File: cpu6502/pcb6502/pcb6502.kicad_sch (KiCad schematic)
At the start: 45 parts, among them J1 Power, J2 RS232, SW1 Reset, SW2 IRQ, SW3 Debug, U1 6502 (CPU), U2 28C256 (ROM), U3 62256 (RAM), U4 6522 (VIA), U5 74HC00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

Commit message: everything is working well!  OS still wip but pretty good
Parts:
- added J3: VIA PB, Connector_PinHeader_2.54mm:PinHeader_2x05_P2.54mm_Vertical, symbol Connector:Conn_01x10_Pin
- added J4: Reset Ext, Connector_PinHeader_2.54mm:PinHeader_1x02_P2.54mm_Vertical, symbol Connector:Conn_01x02_Pin
- C2, C3, C4, C5, C6: footprint Capacitor_THT:C_Disc_D3.0mm_W1.6mm_P2.50mm -> Capacitor_THT:C_Disc_D5.0mm_W2.5mm_P5.00mm
- R5: footprint Resistor_THT:R_Axial_DIN0204_L3.6mm_D1.6mm_P7.62mm_Horizontal -> Resistor_THT:R_Axial_DIN0204_L3.6mm_D1.6mm_P2.54mm_Vertical
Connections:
- net +5V: now also J3.9 (Pin_9)
- net GND: now also J3.10 (Pin_10), J4.2 (Pin_2)
- net RST: now also J4.1 (Pin_1)
- net PB0: now reaches U4.10 (PB0)
- net PB0: now also J3.1 (Pin_1)
- net PB1: now reaches U4.11 (PB1)
- net PB1: now also J3.2 (Pin_2)
- net PB2: now reaches U4.12 (PB2)
- net PB2: now also J3.3 (Pin_3)
- net PB3: now reaches U4.13 (PB3)
- net PB3: now also J3.4 (Pin_4)
- net PB4: now reaches U4.14 (PB4)
- net PB4: now also J3.5 (Pin_5)
- net PB5: now reaches U4.15 (PB5)
- net PB5: now also J3.6 (Pin_6)
- net PB6: now reaches U4.16 (PB6)
- net PB6: now also J3.7 (Pin_7)
- net PB7: now reaches U4.17 (PB7)
- net PB7: now also J3.8 (Pin_8)
- no-connect marks 39 -> 31

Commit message: check point
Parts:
- removed D10: 4, LED_THT:LED_D3.0mm, symbol Device:LED
- removed D11: 5, LED_THT:LED_D3.0mm, symbol Device:LED
- removed D12: 6, LED_THT:LED_D3.0mm, symbol Device:LED
- removed D13: 7, LED_THT:LED_D3.0mm, symbol Device:LED
- removed D5: 0, LED_THT:LED_D3.0mm, symbol Device:LED
- removed D6: 1, LED_THT:LED_D3.0mm, symbol Device:LED
- removed D8: 2, LED_THT:LED_D3.0mm, symbol Device:LED
- removed D9: 3, LED_THT:LED_D3.0mm, symbol Device:LED
- removed J3: VIA PB, Connector_PinHeader_2.54mm:PinHeader_2x05_P2.54mm_Vertical, symbol Connector:Conn_01x10_Pin
- removed RN1, RN2: 220, Resistor_THT:R_Array_SIP8, symbol Device:R_Network07_US
- removed SW2: IRQ, Button_Switch_THT:SW_DIP_SPSTx03_Slide_9.78x9.8mm_W7.62mm_P2.54mm, symbol Switch:SW_DIP_x03
- added J3: VIA, Connector_PinHeader_2.54mm:PinHeader_2x09_P2.54mm_Vertical, symbol Connector_Generic:Conn_02x09_Odd_Even
- added RN1: Resistor Array 220Ω (3), Resistor_THT:R_Array_SIP6, symbol Device:R_Pack03_SIP
- added SW2: Interrupts, Button_Switch_THT:SW_DIP_SPSTx06_Slide_9.78x17.42mm_W7.62mm_P2.54mm, symbol Switch:SW_DIP_x06
- C2, C3, C4, C5: value 1uf -> 1µF
- C6: value 20pf -> 20pF
- C7: value 1uF -> 1µF
- C8: value 0.1uf -> 0.1µF
- R3: value 1K -> 1KΩ
- R4: value 1M -> 1MΩ
- R5: value 1K -> 1KΩ; footprint Resistor_THT:R_Axial_DIN0204_L3.6mm_D1.6mm_P2.54mm_Vertical -> Resistor_THT:R_Axial_DIN0204_L3.6mm_D1.6mm_P7.62mm_Horizontal
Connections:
- net +5V: now also J3.17 (Pin_17), SW2.12, SW2.7; no longer U1.6 (~{NMI})
- net ACIAIRQ: now also SW2.11, SW2.9
- net GND: now also J3.18 (Pin_18), RN1.1 (R1.1), RN1.3 (R2.1), RN1.5 (R3.1)
- net IRQ: now also SW2.1, SW2.2, SW2.3
- net PA0: now also J3.1 (Pin_1)
- net PA1: now also J3.3 (Pin_3)
- net PA2: now also J3.5 (Pin_5)
- net PA3: now also J3.7 (Pin_7)
- net PA4: now also J3.9 (Pin_9)
- net PA5: now also J3.11 (Pin_11)
- net PA6: now also J3.13 (Pin_13)
- net PA7: now also J3.15 (Pin_15)
- net PB0: now also J3.16 (Pin_16)
- net PB1: now also J3.14 (Pin_14)
- net PB2: now also J3.12 (Pin_12)
- net PB3: now also J3.10 (Pin_10)
- net PB4: now also J3.8 (Pin_8)
- net PB5: now also J3.6 (Pin_6)
- net PB6: now also J3.4 (Pin_4)
- net PB7: now also J3.2 (Pin_2)
- net RNPA0: now also RN1.2 (R1.2)
- net RNPA1: now also RN1.4 (R2.2)
- net RNPA2: now also RN1.6 (R3.2)
- net VIAIRQ: now also SW2.10, SW2.8
- new net NMI: SW2.4, SW2.5, SW2.6, U1.6 (~{NMI})
- no-connect marks 31 -> 28
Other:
- moved on the sheet: D1, D4, D7

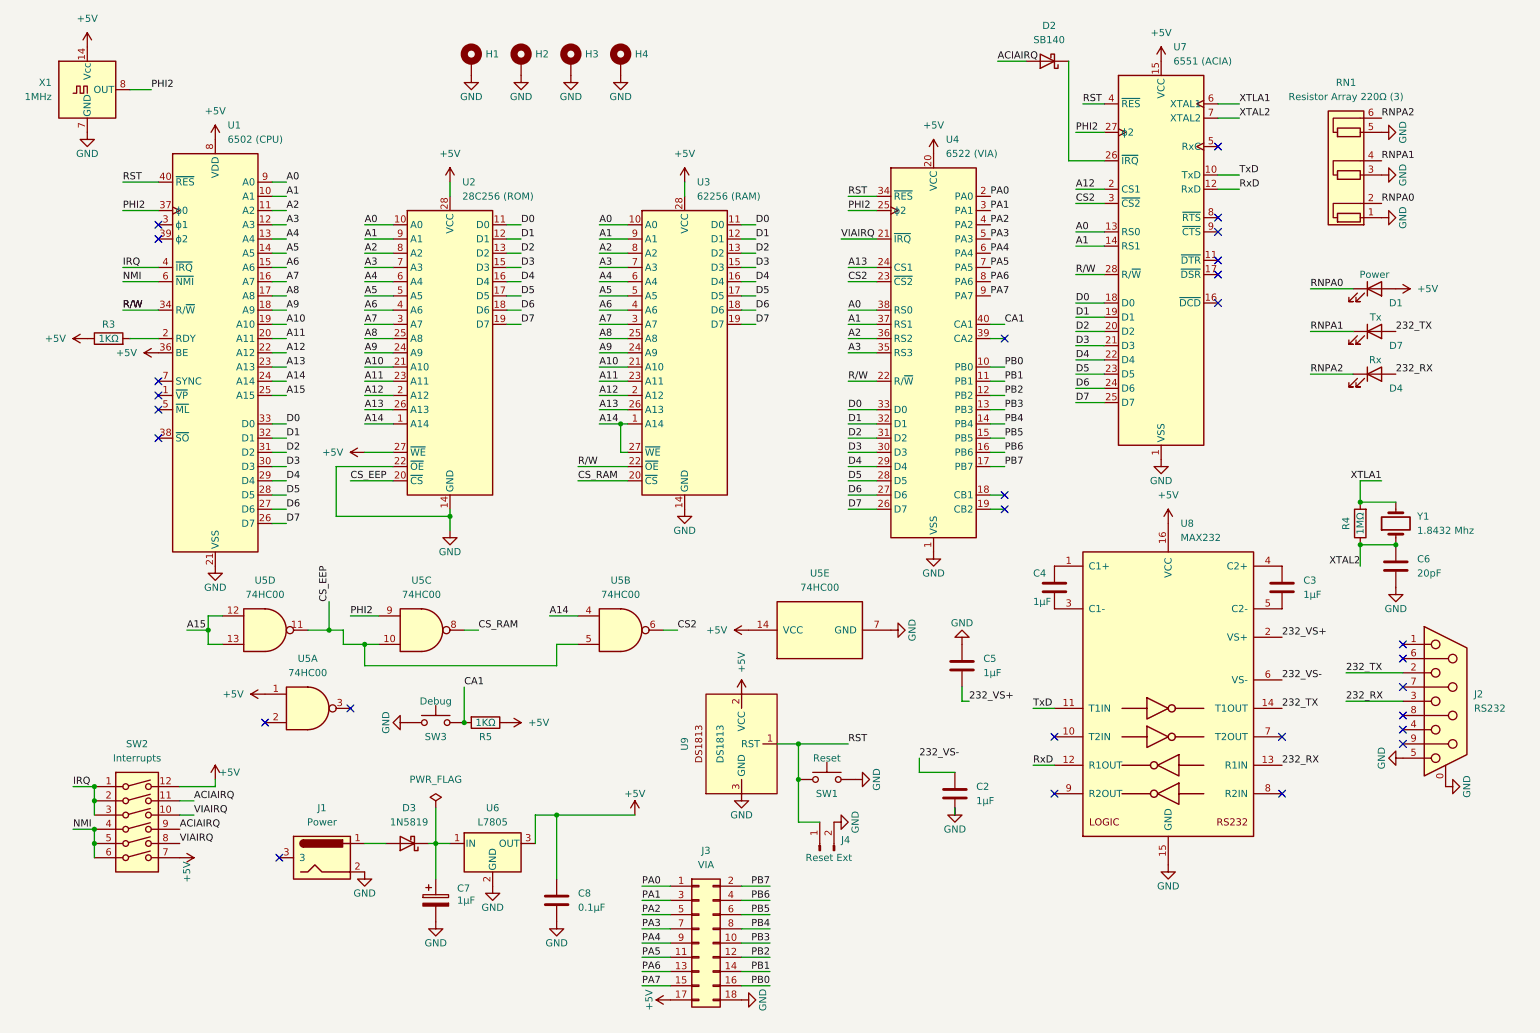
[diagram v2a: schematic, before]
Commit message: rs232 nmi / cts, circuit close to done
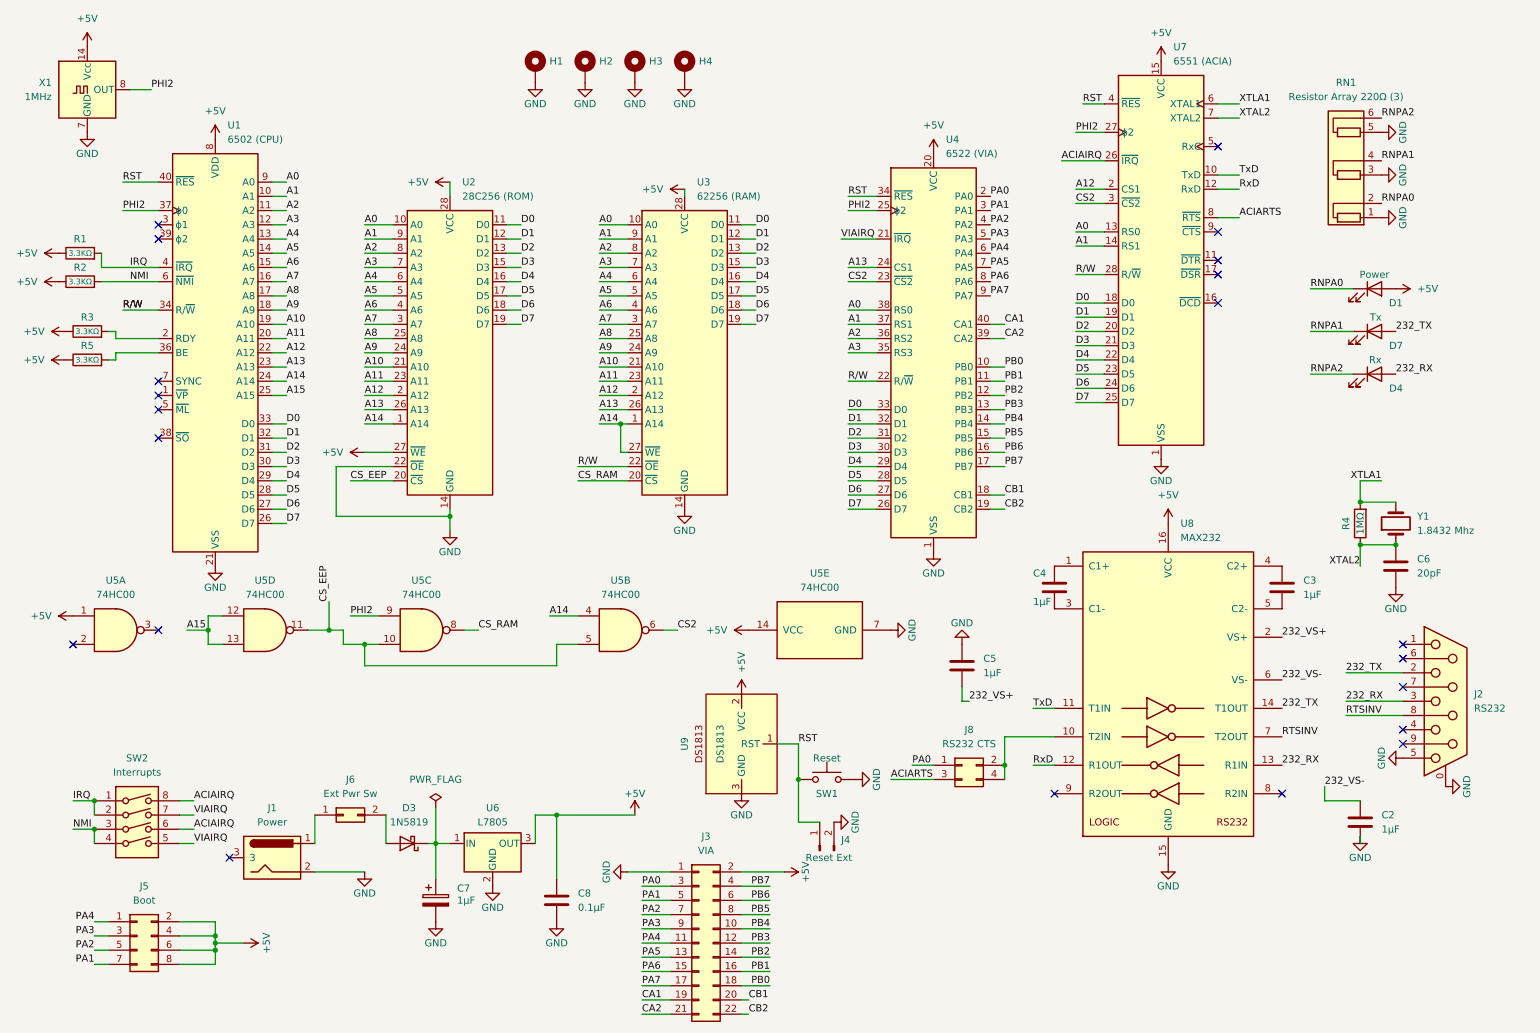
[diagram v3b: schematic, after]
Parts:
- removed D2: SB140, Diode_THT:D_DO-41_SOD81_P10.16mm_Horizontal, symbol Diode:SB140
- removed SW3: Debug, Button_Switch_THT:SW_TH_Tactile_Omron_B3F-10xx, symbol Switch:SW_Push
- added J5: Boot, Connector_PinHeader_2.54mm:PinHeader_2x04_P2.54mm_Vertical, symbol Connector_Generic:Conn_02x04_Odd_Even
- added J6: Ext Pwr Sw, Connector_PinHeader_2.54mm:PinHeader_2x01_P2.54mm_Vertical, symbol Connector_Generic:Conn_02x01
- added J8: RS232 CTS, Connector_PinHeader_2.54mm:PinHeader_2x02_P2.54mm_Vertical, symbol Connector_Generic:Conn_02x02_Odd_Even
- added R1, R2: 3.3KΩ, Resistor_THT:R_Axial_DIN0204_L3.6mm_D1.6mm_P7.62mm_Horizontal, symbol Device:R
- J3: footprint Connector_PinHeader_2.54mm:PinHeader_2x09_P2.54mm_Vertical -> Connector_PinHeader_2.54mm:PinHeader_2x11_P2.54mm_Vertical; symbol Connector_Generic:Conn_02x09_Odd_Even -> Connector_Generic:Conn_02x11_Odd_Even
- R3, R5: value 1KΩ -> 3.3KΩ
- SW2: footprint Button_Switch_THT:SW_DIP_SPSTx06_Slide_9.78x17.42mm_W7.62mm_P2.54mm -> Button_Switch_THT:SW_DIP_SPSTx04_Slide_9.78x12.34mm_W7.62mm_P2.54mm; symbol Switch:SW_DIP_x06 -> Switch:SW_DIP_x04
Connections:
- net +5V: now also J3.2 (Pin_2), J5.2 (Pin_2), J5.4 (Pin_4), J5.6 (Pin_6), J5.8 (Pin_8), R1.1, R2.1; no longer J3.17 (Pin_17), SW2.12, SW2.7, U1.36 (BE)
- net ACIAIRQ: now also SW2.6, SW2.8, U7.26 (~{IRQ}); no longer SW2.11, SW2.9
- net CA1: now also J3.19 (Pin_19); no longer R5.2
- net GND: now also J3.1 (Pin_1); no longer J3.18 (Pin_18)
- net IRQ: now also R1.2; no longer SW2.3
- net NMI: now also SW2.3, R2.2; no longer SW2.5, SW2.6
- net PA0: now also J3.3 (Pin_3), J8.1 (Pin_1); no longer J3.1 (Pin_1)
- net PA1: now also J3.5 (Pin_5), J5.7 (Pin_7); no longer J3.3 (Pin_3)
- net PA2: now also J3.7 (Pin_7), J5.5 (Pin_5); no longer J3.5 (Pin_5)
- net PA3: now also J3.9 (Pin_9), J5.3 (Pin_3); no longer J3.7 (Pin_7)
- net PA4: now also J3.11 (Pin_11), J5.1 (Pin_1); no longer J3.9 (Pin_9)
- net PA5: now also J3.13 (Pin_13); no longer J3.11 (Pin_11)
- net PA6: now also J3.15 (Pin_15); no longer J3.13 (Pin_13)
- net PA7: now also J3.17 (Pin_17); no longer J3.15 (Pin_15)
- net PB0: now also J3.18 (Pin_18); no longer J3.16 (Pin_16)
- net PB1: now also J3.16 (Pin_16); no longer J3.14 (Pin_14)
- net PB2: now also J3.14 (Pin_14); no longer J3.12 (Pin_12)
- net PB3: now also J3.12 (Pin_12); no longer J3.10 (Pin_10)
- net PB4: now also J3.10 (Pin_10); no longer J3.8 (Pin_8)
- net PB5: now also J3.8 (Pin_8); no longer J3.6 (Pin_6)
- net PB6: now also J3.6 (Pin_6); no longer J3.4 (Pin_4)
- net PB7: now also J3.4 (Pin_4); no longer J3.2 (Pin_2)
- net VIAIRQ: now also SW2.5, SW2.7; no longer SW2.10, SW2.8
- net ACIARTS: now reaches U7.8 (~{RTS})
- net ACIARTS: now also J8.3 (Pin_3)
- net at D3.2 (A): now also J6.2 (Pin_2); no longer J1.1
- net at U8.10 (T2IN): now also J8.2 (Pin_2), J8.4 (Pin_4)
- net RTSINV: now reaches U8.7 (T2OUT)
- net RTSINV: now also J2.8
- net CB1: now reaches U4.18 (CB1)
- net CB1: now also J3.20 (Pin_20)
- net CB2: now reaches U4.19 (CB2)
- net CB2: now also J3.22 (Pin_22)
- net CA2: now reaches U4.39 (CA2)
- net CA2: now also J3.21 (Pin_21)
- new net: R5.2, U1.36 (BE)
- new net: J1.1, J6.1 (Pin_1)
- no-connect marks 28 -> 21
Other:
- moved on the sheet: C2, H1, H2, H3, H4, J1, R3, U5A

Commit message: pcb updates
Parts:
- removed RN1: Resistor Array 220Ω (3), Resistor_THT:R_Array_SIP6, symbol Device:R_Pack03_SIP
- removed SW2: Interrupts, Button_Switch_THT:SW_DIP_SPSTx04_Slide_9.78x12.34mm_W7.62mm_P2.54mm, symbol Switch:SW_DIP_x04
- added J7: Interrupts, Connector_PinHeader_2.54mm:PinHeader_2x04_P2.54mm_Vertical, symbol Connector_Generic:Conn_02x04_Odd_Even
- added R6, R7, R8: 220Ω, Resistor_THT:R_Axial_DIN0204_L3.6mm_D1.6mm_P2.54mm_Vertical, symbol Device:R
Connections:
- net ACIAIRQ: now also J7.2 (Pin_2), J7.6 (Pin_6)
- net GND: now also U7.11 (~{DTR}), U7.16 (~{DCD}), U7.17 (~{DSR}), U7.9 (~{CTS}), R6.2, R7.2, R8.2
- net IRQ: now also J7.1 (Pin_1), J7.3 (Pin_3)
- net NMI: now also J7.5 (Pin_5), J7.7 (Pin_7)
- net RNPA0: now also R8.1
- net RNPA1: now also R7.1
- net RNPA2: now also R6.1
- net VIAIRQ: now also J7.4 (Pin_4), J7.8 (Pin_8)
- no-connect marks 21 -> 17
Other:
- moved on the sheet: H1, H2, H3, H4
